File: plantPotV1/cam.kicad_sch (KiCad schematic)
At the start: 4 parts, among them U4 MAX98306xDT

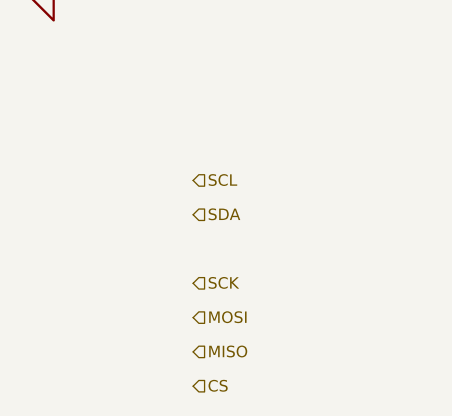
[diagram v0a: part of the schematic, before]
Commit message: updated circuit diagram (top only)
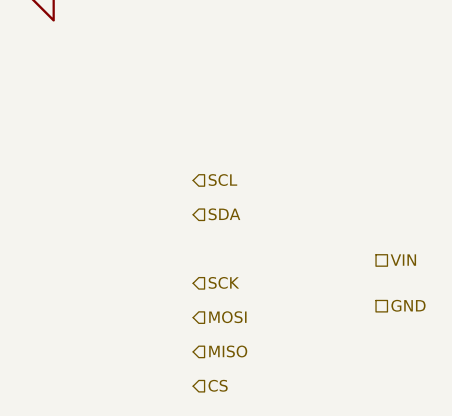
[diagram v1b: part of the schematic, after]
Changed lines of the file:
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@@
+		)
+	)
+	(hierarchical_label "VIN"
+		(shape passive)
+		(at 171.45 115.57 0)
+		(fields_autoplaced yes)
+		(effects
+			(font
+				(size 1.27 1.27)
+			)
+			(justify left)
 		)
 	)
@@
 		(fields_autoplaced yes)
 		(effects
+			(font
+				(size 1.27 1.27)
+			)
+			(justify left)
+		)
+	)
+	(hierarchical_label "GND"
+		(shape passive)
+		(at 171.45 120.65 0)
+		(fields_autoplaced yes)
+		(effects
